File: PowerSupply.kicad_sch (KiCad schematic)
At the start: 42 parts, among them Q201 BSS138, Q202 SQJA62EP-T1_GE3, U201 LM3478MM, U202 MCP1703A-3302

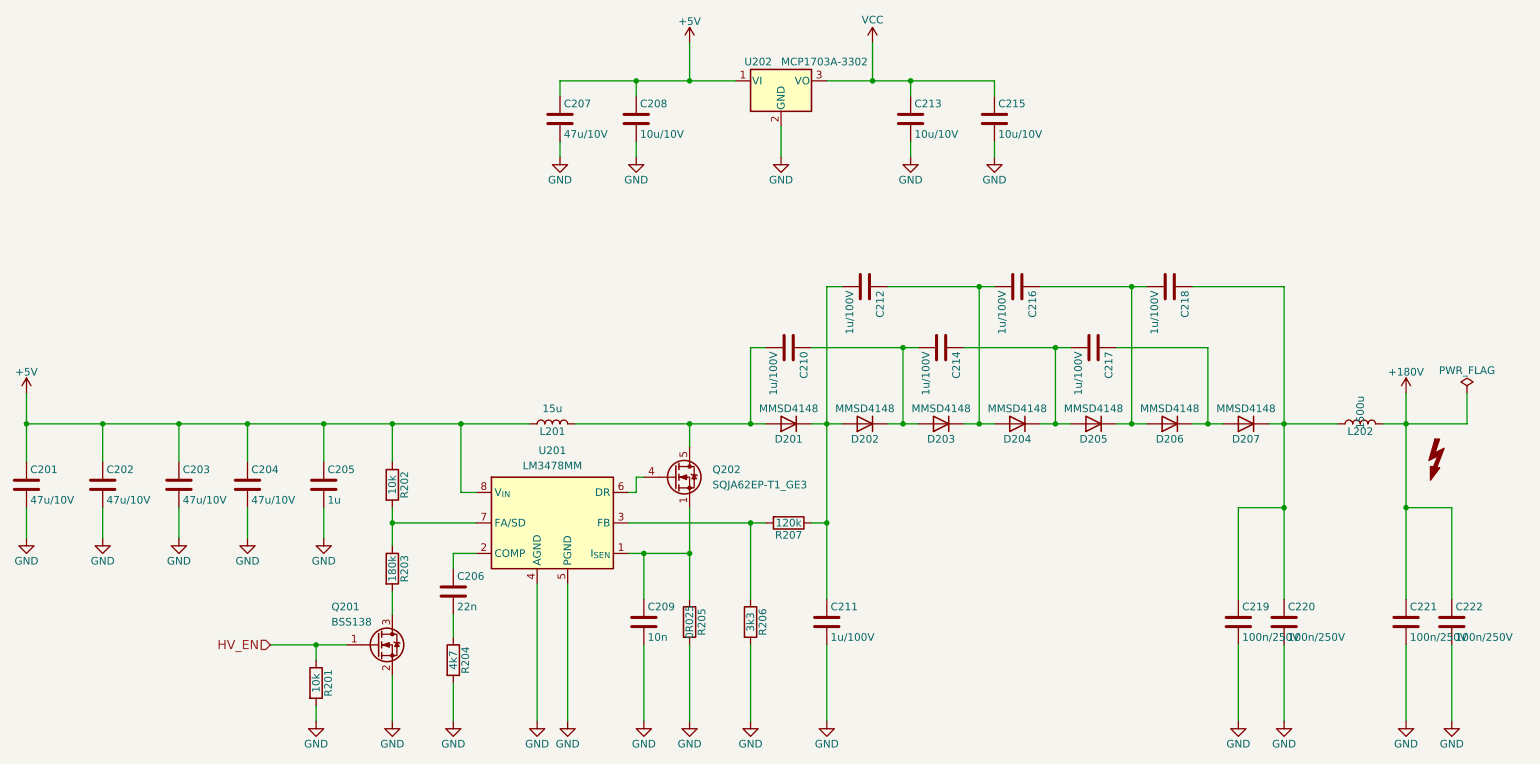
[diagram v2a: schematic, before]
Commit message: BoM: optimize parts
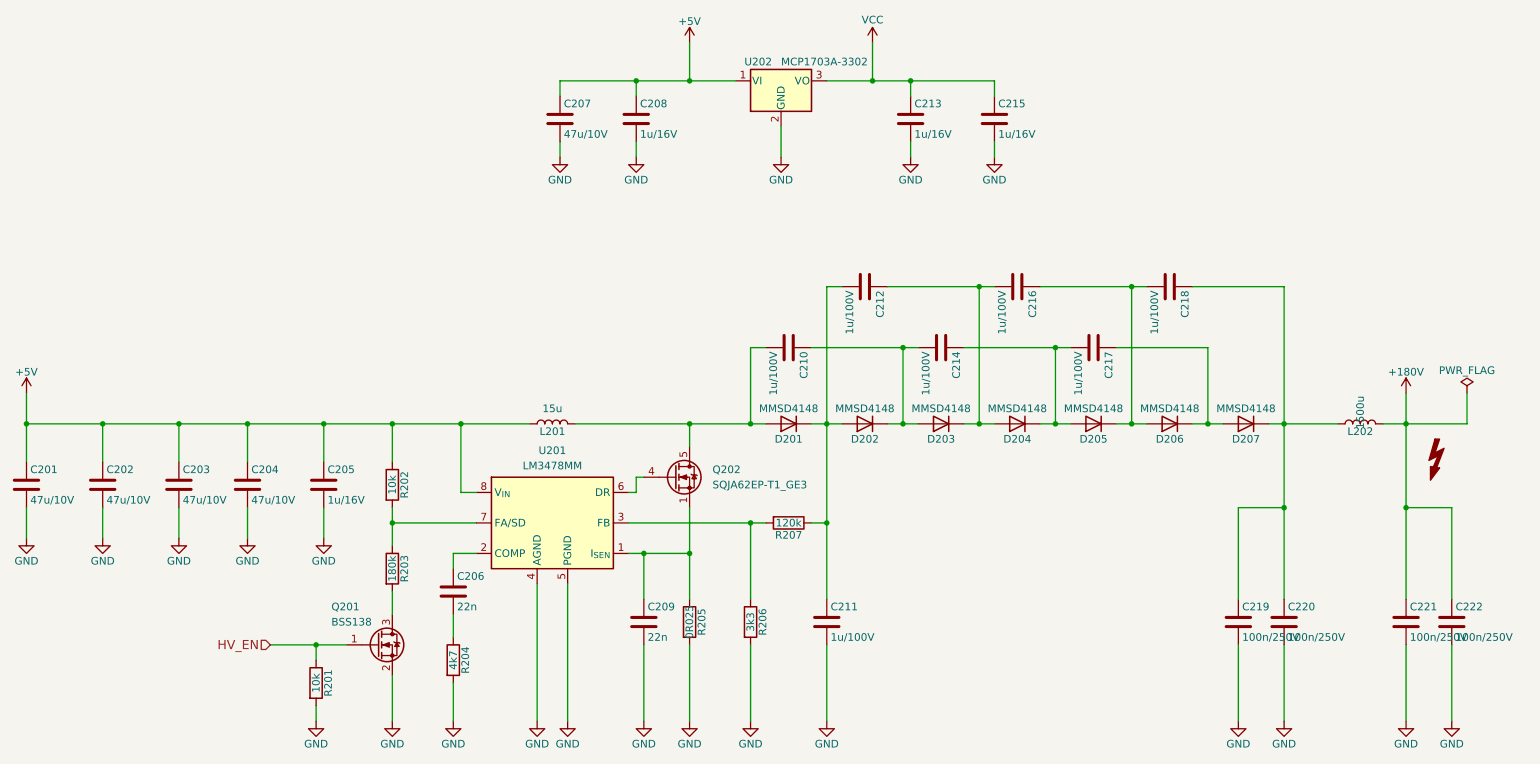
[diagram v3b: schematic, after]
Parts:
- C205: value 1u -> 1u/16V
- C208, C213, C215: value 10u/10V -> 1u/16V; footprint Capacitor_SMD:C_1206_3216Metric -> Capacitor_SMD:C_0805_2012Metric; SPN CL21B103KBANNNC -> CL21B105KOFNNNE
- C209: value 10n -> 22n; SPN CL10B105KO8NNNC -> CC0805KRX7R9BB223
- L201: SPN HPI1260-150 -> DR125-150-R
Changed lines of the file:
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@@
       (effects (font (size 1.27 1.27)) hide)
     )
-    (property "SPN" "HPI1260-150" (at 111.76 95.25 0)
+    (property "SPN" "DR125-150-R" (at 111.76 95.25 0)
       (effects (font (size 1.27 1.27)) hide)
     )
@@
       (effects (font (size 1.27 1.27)) (justify left))
     )
-    (property "Value" "10u/10V" (at 172.085 46.99 0)
-      (effects (font (size 1.27 1.27)) (justify left))
-    )
-    (property "Footprint" "Capacitor_SMD:C_1206_3216Metric" (at 172.4152 48.26 0)
+    (property "Value" "1u/16V" (at 172.085 46.99 0)
+      (effects (font (size 1.27 1.27)) (justify left))
+    )
+    (property "Footprint" "Capacitor_SMD:C_0805_2012Metric" (at 172.4152 48.26 0)
       (effects (font (size 1.27 1.27)) hide)
     )
@@
       (effects (font (size 1.27 1.27)) hide)
     )
-    (property "SPN" "CL21B103KBANNNC" (at 171.45 44.45 0)
+    (property "SPN" "CL21B105KOFNNNE" (at 171.45 44.45 0)
       (effects (font (size 1.27 1.27)) hide)
     )
@@
       (effects (font (size 1.27 1.27)) (justify left))
     )
-    (property "Value" "1u" (at 74.295 107.95 0)
+    (property "Value" "1u/16V" (at 74.295 107.95 0)
       (effects (font (size 1.27 1.27)) (justify left))
     )
@@
       (effects (font (size 1.27 1.27)) (justify left))
     )
-    (property "Value" "10u/10V" (at 186.055 46.99 0)
-      (effects (font (size 1.27 1.27)) (justify left))
-    )
-    (property "Footprint" "Capacitor_SMD:C_1206_3216Metric" (at 186.3852 48.26 0)
+    (property "Value" "1u/16V" (at 186.055 46.99 0)
+      (effects (font (size 1.27 1.27)) (justify left))
+    )
+    (property "Footprint" "Capacitor_SMD:C_0805_2012Metric" (at 186.3852 48.26 0)
       (effects (font (size 1.27 1.27)) hide)
     )
@@
       (effects (font (size 1.27 1.27)) hide)
     )
-    (property "SPN" "CL21B103KBANNNC" (at 185.42 44.45 0)
+    (property "SPN" "CL21B105KOFNNNE" (at 185.42 44.45 0)
       (effects (font (size 1.27 1.27)) hide)
     )
@@
       (effects (font (size 1.27 1.27)) (justify left))
     )
-    (property "Value" "10u/10V" (at 126.365 46.99 0)
-      (effects (font (size 1.27 1.27)) (justify left))
-    )
-    (property "Footprint" "Capacitor_SMD:C_1206_3216Metric" (at 126.6952 48.26 0)
+    (property "Value" "1u/16V" (at 126.365 46.99 0)
+      (effects (font (size 1.27 1.27)) (justify left))
+    )
+    (property "Footprint" "Capacitor_SMD:C_0805_2012Metric" (at 126.6952 48.26 0)
       (effects (font (size 1.27 1.27)) hide)
     )
@@
       (effects (font (size 1.27 1.27)) hide)
     )
-    (property "SPN" "CL21B103KBANNNC" (at 125.73 44.45 0)
+    (property "SPN" "CL21B105KOFNNNE" (at 125.73 44.45 0)
       (effects (font (size 1.27 1.27)) hide)
     )
@@
       (effects (font (size 1.27 1.27)) (justify left))
     )
-    (property "Value" "10n" (at 127.635 130.81 0)
+    (property "Value" "22n" (at 127.635 130.81 0)
       (effects (font (size 1.27 1.27)) (justify left))
     )
@@
       (effects (font (size 1.27 1.27)) hide)
     )
-    (property "SPN" "CL10B105KO8NNNC" (at 127 128.27 0)
-      (effects (font (size 1.27 1.27)) hide)
-    )
+    (property "SPN" "CC0805KRX7R9BB223" (at 127 128.27 0)
+      (effects (font (size 1.27 1.27)) hide)
+    )

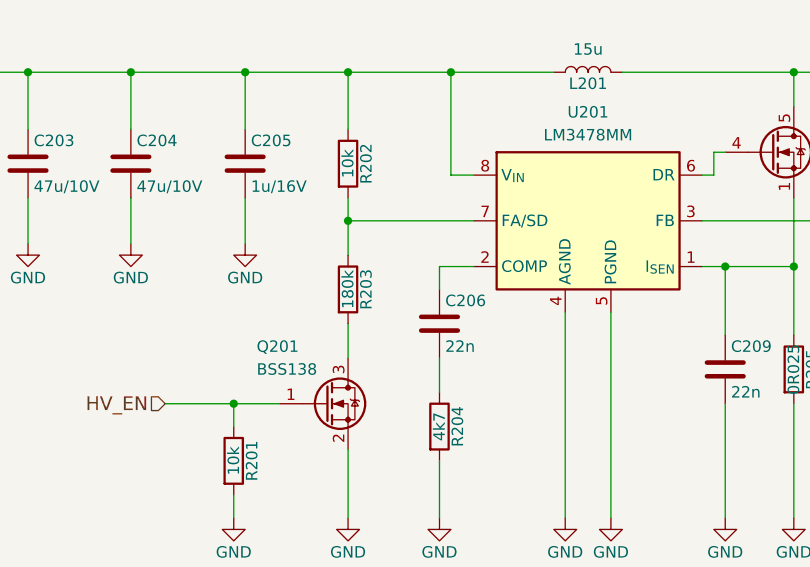
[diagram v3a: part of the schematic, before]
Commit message: pcb: fix HV generator enable input
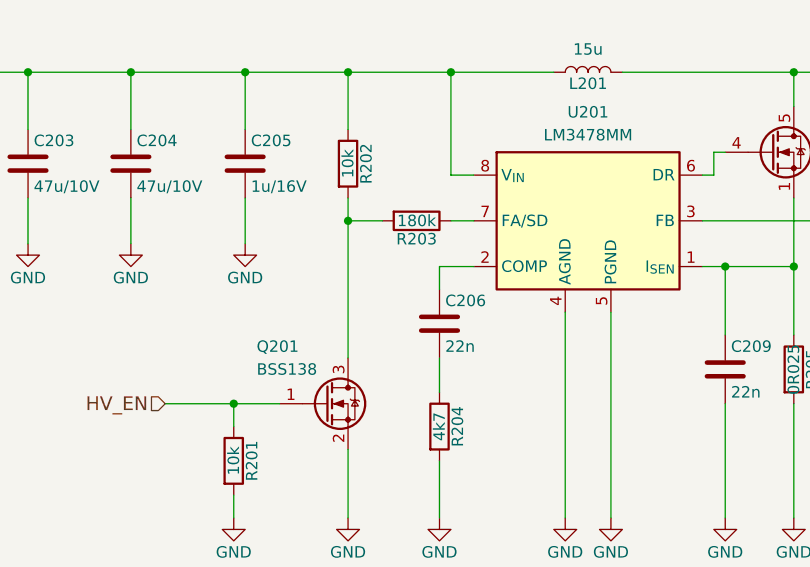
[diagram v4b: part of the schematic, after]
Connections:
- net at R203.1, U201.7 (FA/SD): no longer R202.2
- net at Q201.3 (D), R203.2: now also R202.2
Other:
- moved on the sheet: R203
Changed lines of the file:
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@@
   (title_block
     (title "ZM108x, Z57x nixieboard")
-    (date "2025-09-04")
-    (rev "3/${GITHASH}")
+    (date "2026-02-27")
+    (rev "2.1/${GITHASH}")
     (comment 1 "Atuthor: Martin Sabol")
   )
@@
   (junction (at 165.1 38.1) (diameter 0) (color 0 0 0 0)
   )
+  (junction (at 85.09 111.76) (diameter 0) (color 0 0 0 0)
+  )
   (junction (at 220.98 95.25) (diameter 0) (color 0 0 0 0)
   )
@@
   (junction (at 195.58 82.55) (diameter 0) (color 0 0 0 0)
   )
-  (junction (at 85.09 111.76) (diameter 0) (color 0 0 0 0)
-  )
   (junction (at 73.66 95.25) (diameter 0) (color 0 0 0 0)
   )
@@
     (stroke (width 0) (type default))
   )
+  (wire (pts (xy 85.09 109.22) (xy 85.09 111.76))
+    (stroke (width 0) (type default))
+  )
   (wire (pts (xy 124.46 116.84) (xy 127 116.84))
     (stroke (width 0) (type default))
@@
     (stroke (width 0) (type default))
   )
-  (wire (pts (xy 99.06 111.76) (xy 85.09 111.76))
+  (wire (pts (xy 99.06 111.76) (xy 96.52 111.76))
     (stroke (width 0) (type default))
   )
@@
     (stroke (width 0) (type default))
   )
-  (wire (pts (xy 85.09 109.22) (xy 85.09 111.76))
+  (wire (pts (xy 85.09 111.76) (xy 85.09 127))
     (stroke (width 0) (type default))
   )
@@
     (stroke (width 0) (type default))
   )
-  (wire (pts (xy 85.09 111.76) (xy 85.09 115.57))
-    (stroke (width 0) (type default))
-  )
   (wire (pts (xy 109.22 121.92) (xy 109.22 144.78))
     (stroke (width 0) (type default))
@@
     (stroke (width 0) (type default))
   )
-  (wire (pts (xy 85.09 123.19) (xy 85.09 127))
-    (stroke (width 0) (type default))
-  )
   (wire (pts (xy 170.18 82.55) (xy 170.18 95.25))
     (stroke (width 0) (type default))
@@
   )
   (wire (pts (xy 36.83 109.22) (xy 36.83 114.3))
+    (stroke (width 0) (type default))
+  )
+  (wire (pts (xy 88.9 111.76) (xy 85.09 111.76))
     (stroke (width 0) (type default))
   )
@@
     )
   )
-  (symbol (lib_id "Device:R") (at 85.09 119.38 0) (unit 1)
-    (in_bom yes) (on_board yes) (dnp no)
-    (property "Reference" "R203" (at 87.122 119.38 90)
-      (effects (font (size 1.27 1.27)))
-    )
-    (property "Value" "180k" (at 85.09 119.38 90)
-      (effects (font (size 1.27 1.27)))
-    )
-    (property "Footprint" "Resistor_SMD:R_0805_2012Metric" (at 83.312 119.38 90)
-      (effects (font (size 1.27 1.27)) hide)
-    )
-    (property "Datasheet" "~" (at 85.09 119.38 0)
-      (effects (font (size 1.27 1.27)) hide)
-    )
-    (property "Supplier" "TME" (at 85.09 119.38 0)
-      (effects (font (size 1.27 1.27)) hide)
-    )
-    (property "SPN" "0805S8F1803T5E" (at 85.09 119.38 0)
-      (effects (font (size 1.27 1.27)) hide)
-    )
+  (symbol (lib_id "Device:R") (at 92.71 111.76 270) (unit 1)
+    (in_bom yes) (on_board yes) (dnp no)
+    (property "Reference" "R203" (at 92.71 113.792 90)
+      (effects (font (size 1.27 1.27)))
+    )
+    (property "Value" "180k" (at 92.71 111.76 90)
+      (effects (font (size 1.27 1.27)))
+    )
+    (property "Footprint" "Resistor_SMD:R_0805_2012Metric" (at 92.71 109.982 90)
+      (effects (font (size 1.27 1.27)) hide)
+    )
+    (property "Datasheet" "~" (at 92.71 111.76 0)
+      (effects (font (size 1.27 1.27)) hide)
+    )
+    (property "Supplier" "TME" (at 92.71 111.76 0)
+      (effects (font (size 1.27 1.27)) hide)
+    )
+    (property "SPN" "0805S8F1803T5E" (at 92.71 111.76 0)
+      (effects (font (size 1.27 1.27)) hide)
+    )
